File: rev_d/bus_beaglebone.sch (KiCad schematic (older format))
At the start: 47 parts, among them J1 TERMINATE_JUMPER, J2 LED_JUMPER, SW1 MJTP1243, U1 MCP7940, U2 74HCT08, U3 MCP2562, U4 L78L05AC, U5 ATMEGA324_DIP40, U6 L78L33AC, X1 16MHz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

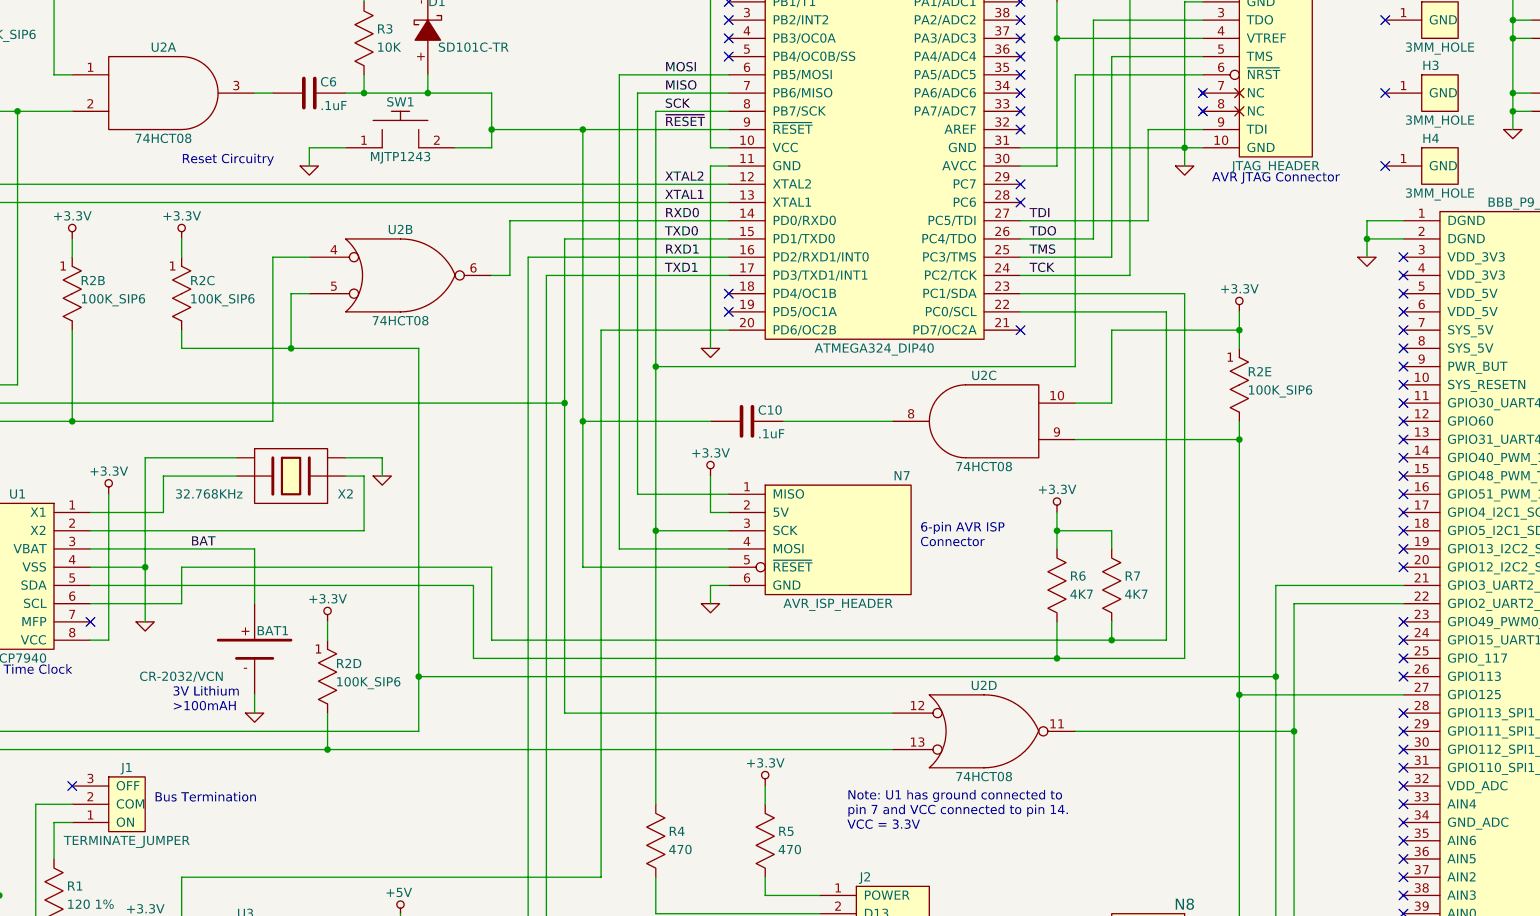
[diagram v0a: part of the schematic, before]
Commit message: Converted 74HCT08 => 74HC08.
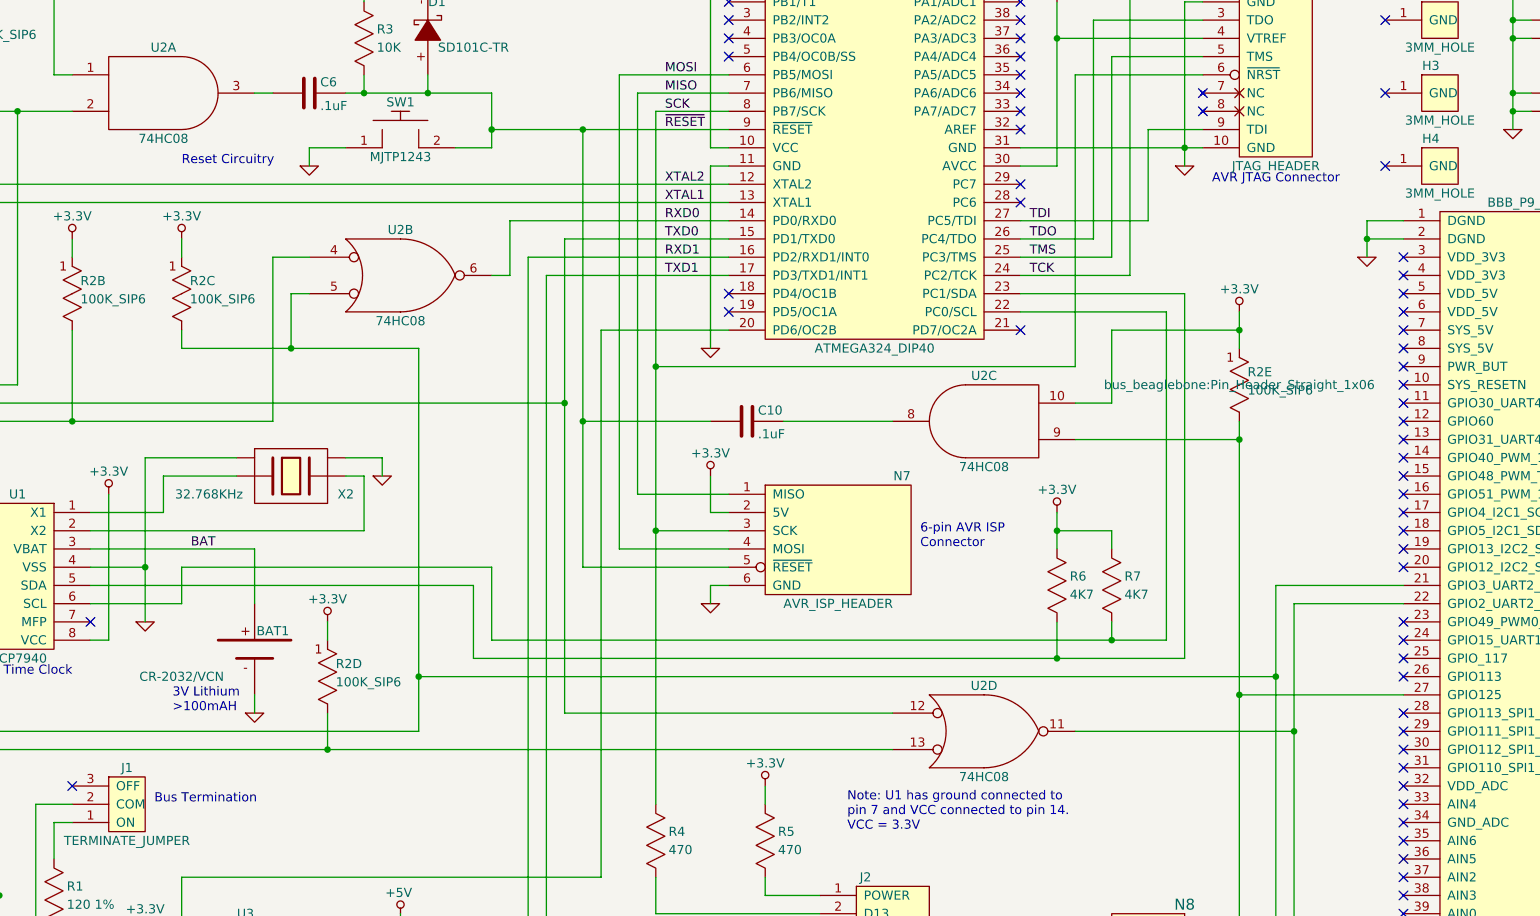
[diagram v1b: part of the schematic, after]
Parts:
- R2: footprint ~ -> bus_beaglebone:Pin_Header_Straight_1x06
- U2: value 74HCT08 -> 74HC08
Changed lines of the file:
@@
 $EndComp
 $Comp
-L GND #PWR02
+L GND #PWR01
 U 1 1 53E3C25F
 P 8100 1900
-F 0 "#PWR02" H 8100 1900 30  0001 C CNN
+F 0 "#PWR01" H 8100 1900 30  0001 C CNN
 F 1 "GND" H 8100 1830 30  0001 C CNN
 F 2 "" H 8100 1900 60  0000 C CNN
@@
 $EndComp
 $Comp
-L GND #PWR03
+L GND #PWR02
 U 1 1 53E3C850
 P 600 2700
-F 0 "#PWR03" H 600 2700 30  0001 C CNN
+F 0 "#PWR02" H 600 2700 30  0001 C CNN
 F 1 "GND" H 600 2630 30  0001 C CNN
 F 2 "" H 600 2700 60  0000 C CNN
@@
 $EndComp
 $Comp
-L GND #PWR04
+L GND #PWR03
 U 1 1 53E3C865
 P 1400 2700
-F 0 "#PWR04" H 1400 2700 30  0001 C CNN
+F 0 "#PWR03" H 1400 2700 30  0001 C CNN
 F 1 "GND" H 1400 2630 30  0001 C CNN
 F 2 "" H 1400 2700 60  0000 C CNN
@@
 $EndComp
 $Comp
-L GND #PWR05
+L GND #PWR04
 U 1 1 53E3ED67
 P 3950 6500
-F 0 "#PWR05" H 3950 6500 30  0001 C CNN
+F 0 "#PWR04" H 3950 6500 30  0001 C CNN
 F 1 "GND" H 3950 6430 30  0001 C CNN
 F 2 "" H 3950 6500 60  0000 C CNN
@@
 $EndComp
 $Comp
-L GND #PWR06
+L GND #PWR05
 U 1 1 53E4026A
 P 1400 5500
-F 0 "#PWR06" H 1400 5500 30  0001 C CNN
+F 0 "#PWR05" H 1400 5500 30  0001 C CNN
 F 1 "GND" H 1400 5430 30  0001 C CNN
 F 2 "" H 1400 5500 60  0000 C CNN
@@
 $EndComp
 $Comp
-L GND #PWR07
+L GND #PWR06
 U 1 1 53E406BF
 P 1400 3700
-F 0 "#PWR07" H 1400 3700 30  0001 C CNN
+F 0 "#PWR06" H 1400 3700 30  0001 C CNN
 F 1 "GND" H 1400 3630 30  0001 C CNN
 F 2 "" H 1400 3700 60  0000 C CNN
@@
 P 3800 2500
 F 0 "U2" H 3800 2750 50  0000 C CNN
-F 1 "74HCT08" H 3800 2250 50  0000 C CNN
+F 1 "74HC08" H 3800 2250 50  0000 C CNN
 F 2 "bus_beaglebone:DIP-14__300" H 3800 2500 60  0001 C CNN
 F 3 "" H 3800 2500 60  0000 C CNN
@@
 P 7000 5000
 F 0 "U2" H 7000 5250 50  0000 C CNN
-F 1 "74HCT08" H 7000 4750 50  0000 C CNN
+F 1 "74HC08" H 7000 4750 50  0000 C CNN
 F 2 "bus_beaglebone:DIP-14__300" H 7000 5000 60  0001 C CNN
 F 3 "" H 7000 5000 60  0000 C CNN
@@
 $EndComp
 $Comp
-L GND #PWR08
+L GND #PWR07
 U 1 1 53E41588
 P 8500 6500
-F 0 "#PWR08" H 8500 6500 30  0001 C CNN
+F 0 "#PWR07" H 8500 6500 30  0001 C CNN
 F 1 "GND" H 8500 6430 30  0001 C CNN
 F 2 "" H 8500 6500 60  0000 C CNN
@@
 NoConn ~ -2850 4150
 $Comp
-L GND #PWR09
+L GND #PWR08
 U 1 1 53E4BEB5
 P 3300 1900
-F 0 "#PWR09" H 3300 1900 30  0001 C CNN
+F 0 "#PWR08" H 3300 1900 30  0001 C CNN
 F 1 "GND" H 3300 1830 30  0001 C CNN
 F 2 "" H 3300 1900 60  0000 C CNN
@@
 $EndComp
 $Comp
-L GND #PWR010
+L GND #PWR09
 U 1 1 53E4C9AF
 P 5500 2900
-F 0 "#PWR010" H 5500 2900 30  0001 C CNN
+F 0 "#PWR09" H 5500 2900 30  0001 C CNN
 F 1 "GND" H 5500 2830 30  0001 C CNN
 F 2 "" H 5500 2900 60  0000 C CNN
@@
 $EndComp
 $Comp
-L GND #PWR011
+L GND #PWR010
 U 1 1 53E42028
 P 5500 4300
-F 0 "#PWR011" H 5500 4300 30  0001 C CNN
+F 0 "#PWR010" H 5500 4300 30  0001 C CNN
 F 1 "GND" H 5500 4230 30  0001 C CNN
 F 2 "" H 5500 4300 60  0000 C CNN
@@
 NoConn ~ 7200 1700
 $Comp
-L +5V #PWR012
+L +5V #PWR011
 U 1 1 53E5079A
 P 2800 7000
-F 0 "#PWR012" H 2800 7090 20  0001 C CNN
+F 0 "#PWR011" H 2800 7090 20  0001 C CNN
 F 1 "+5V" H 2790 7115 50  0000 C CNN
 F 2 "" H 2800 7000 60  0000 C CNN
@@
 $EndComp
 $Comp
-L GND #PWR013
+L GND #PWR012
 U 1 1 53E64F41
 P 6000 6900
-F 0 "#PWR013" H 6000 6900 30  0001 C CNN
+F 0 "#PWR012" H 6000 6900 30  0001 C CNN
 F 1 "GND" H 6000 6830 30  0001 C CNN
 F 2 "" H 6000 6900 60  0000 C CNN
@@
 P 2500 1500
 F 0 "U2" H 2500 1750 50  0000 C CNN
-F 1 "74HCT08" H 2500 1250 50  0000 C CNN
+F 1 "74HC08" H 2500 1250 50  0000 C CNN
 F 2 "bus_beaglebone:DIP-14__300" H 2500 1500 60  0001 C CNN
 F 3 "" H 2500 1500 60  0000 C CNN
@@
 P 7000 3300
 F 0 "U2" H 7000 3050 50  0000 C CNN
-F 1 "74HCT08" H 7000 3550 50  0000 C CNN
+F 1 "74HC08" H 7000 3550 50  0000 C CNN
 F 2 "bus_beaglebone:DIP-14__300" H 7000 3300 60  0001 C CNN
 F 3 "" H 7000 3300 60  0000 C CNN
@@
 $EndComp
 $Comp
-L GND #PWR014
+L GND #PWR013
 U 1 1 53E8748B
 P 9100 2400
-F 0 "#PWR014" H 9100 2400 30  0001 C CNN
+F 0 "#PWR013" H 9100 2400 30  0001 C CNN
 F 1 "GND" H 9100 2330 30  0001 C CNN
 F 2 "" H 9100 2400 60  0000 C CNN
@@
 $EndComp
 $Comp
-L GND #PWR015
+L GND #PWR014
 U 1 1 5443768F
 P 3000 4900
-F 0 "#PWR015" H 3000 4900 30  0001 C CNN
+F 0 "#PWR014" H 3000 4900 30  0001 C CNN
 F 1 "GND" H 3000 4830 30  0001 C CNN
 F 2 "" H 3000 4900 60  0000 C CNN
@@
 $EndComp
 $Comp
-L GND #PWR016
+L GND #PWR015
 U 1 1 5443780C
 P 2400 4400
-F 0 "#PWR016" H 2400 4400 30  0001 C CNN
+F 0 "#PWR015" H 2400 4400 30  0001 C CNN
 F 1 "GND" H 2400 4330 30  0001 C CNN
 F 2 "" H 2400 4400 60  0000 C CNN
@@
 $EndComp
 $Comp
-L +3.3V #PWR017
+L +3.3V #PWR016
 U 1 1 5443A36B
 P 7400 3800
-F 0 "#PWR017" H 7400 3760 30  0001 C CNN
+F 0 "#PWR016" H 7400 3760 30  0001 C CNN
 F 1 "+3.3V" H 7400 3925 50  0000 C CNN
 F 2 "" H 7400 3800 60  0000 C CNN
@@
 $EndComp
 $Comp
-L +3.3V #PWR018
+L +3.3V #PWR017
 U 1 1 5443A423
 P 8400 2700
-F 0 "#PWR018" H 8400 2660 30  0001 C CNN
+F 0 "#PWR017" H 8400 2660 30  0001 C CNN
 F 1 "+3.3V" H 8400 2825 50  0000 C CNN
 F 2 "" H 8400 2700 60  0000 C CNN
@@
 $EndComp
 $Comp
-L +3.3V #PWR019
+L +3.3V #PWR018
 U 1 1 5443A4D3
 P 2200 3700
-F 0 "#PWR019" H 2200 3660 30  0001 C CNN
+F 0 "#PWR018" H 2200 3660 30  0001 C CNN
 F 1 "+3.3V" H 2200 3825 50  0000 C CNN
 F 2 "" H 2200 3700 60  0000 C CNN
@@
 GND
 $Comp
-L GND #PWR020
+L GND #PWR019
 U 1 1 54441157
 P 3700 3600
-F 0 "#PWR020" H 3700 3600 30  0001 C CNN
+F 0 "#PWR019" H 3700 3600 30  0001 C CNN
 F 1 "GND" H 3700 3530 30  0001 C CNN
 F 2 "" H 3700 3600 60  0000 C CNN
@@
 $EndComp
 $Comp
-L GND #PWR021
+L GND #PWR020
 U 1 1 54442992
 P 9900 1700
-F 0 "#PWR021" H 9900 1700 30  0001 C CNN
+F 0 "#PWR020" H 9900 1700 30  0001 C CNN
 F 1 "GND" H 9900 1630 30  0001 C CNN
 F 2 "" H 9900 1700 60  0000 C CNN
@@
 $EndComp
 $Comp
-L +3.3V #PWR022
+L +3.3V #PWR021
 U 1 1 54ADFC43
 P 7400 1000
-F 0 "#PWR022" H 7400 960 30  0001 C CNN
+F 0 "#PWR021" H 7400 960 30  0001 C CNN
 F 1 "+3.3V" H 7400 1125 50  0000 C CNN
 F 2 "" H 7400 1000 60  0000 C CNN
@@
 NoConn ~ 9300 2500
 $Comp
-L +3.3V #PWR023
+L +3.3V #PWR022
 U 1 1 54AE0541
 P 3950 700
-F 0 "#PWR023" H 3950 660 30  0001 C CNN
+F 0 "#PWR022" H 3950 660 30  0001 C CNN
 F 1 "+3.3V" H 3950 825 50  0000 C CNN
 F 2 "" H 3950 700 60  0000 C CNN
@@
 $EndComp
 $Comp
-L +3.3V #PWR024
+L +3.3V #PWR023
 U 1 1 54AE0CA5
 P 1400 850
-F 0 "#PWR024" H 1400 810 30  0001 C CNN
+F 0 "#PWR023" H 1400 810 30  0001 C CNN
 F 1 "+3.3V" H 1400 975 50  0000 C CNN
 F 2 "" H 1400 850 60  0000 C CNN
@@
 $EndComp
 $Comp
-L +3.3V #PWR025
+L +3.3V #PWR024
 U 1 1 54AE0EC4
 P 2000 2300
-F 0 "#PWR025" H 2000 2260 30  0001 C CNN
+F 0 "#PWR024" H 2000 2260 30  0001 C CNN
 F 1 "+3.3V" H 2000 2425 50  0000 C CNN
 F 2 "" H 2000 2300 60  0000 C CNN
@@
 $EndComp
 $Comp
-L +3.3V #PWR026
+L +3.3V #PWR025
 U 1 1 54AE1BC8
 P 2400 6100
-F 0 "#PWR026" H 2400 6060 30  0001 C CNN
+F 0 "#PWR025" H 2400 6060 30  0001 C CNN
 F 1 "+3.3V" H 2400 6225 50  0000 C CNN
 F 2 "" H 2400 6100 60  0000 C CNN
@@
 $EndComp
 $Comp
-L +3.3V #PWR027
+L +3.3V #PWR026
 U 1 1 54AE24EE
 P 5500 3600
-F 0 "#PWR027" H 5500 3560 30  0001 C CNN
+F 0 "#PWR026" H 5500 3560 30  0001 C CNN
 F 1 "+3.3V" H 5500 3725 50  0000 C CNN
 F 2 "" H 5500 3600 60  0000 C CNN
@@
 $EndComp
 $Comp
-L +3.3V #PWR028
+L +3.3V #PWR027
 U 1 1 54AE4768
 P 5800 5300
-F 0 "#PWR028" H 5800 5260 30  0001 C CNN
+F 0 "#PWR027" H 5800 5260 30  0001 C CNN
 F 1 "+3.3V" H 5800 5425 50  0000 C CNN
 F 2 "" H 5800 5300 60  0000 C CNN
@@
 NoConn ~ 9300 4100
 $Comp
-L +3.3V #PWR029
+L +3.3V #PWR028
 U 1 1 54AE64E0
 P 2600 2300
-F 0 "#PWR029" H 2600 2260 30  0001 C CNN
+F 0 "#PWR028" H 2600 2260 30  0001 C CNN
 F 1 "+3.3V" H 2600 2425 50  0000 C CNN
 F 2 "" H 2600 2300 60  0000 C CNN
@@
 $EndComp
 $Comp
-L GND #PWR030
+L GND #PWR029
 U 1 1 54AE368F
 P 2800 7800
-F 0 "#PWR030" H 2800 7800 30  0001 C CNN
+F 0 "#PWR029" H 2800 7800 30  0001 C CNN
 F 1 "GND" H 2800 7730 30  0001 C CNN
 F 2 "" H 2800 7800 60  0000 C CNN
@@
 Extra Serial Connector
 $Comp
-L +3.3V #PWR031
+L +3.3V #PWR030
 U 1 1 54AE44C6
 P 4600 7000
-F 0 "#PWR031" H 4600 6960 30  0001 C CNN
+F 0 "#PWR030" H 4600 6960 30  0001 C CNN
 F 1 "+3.3V" H 4600 7125 50  0000 C CNN
 F 2 "" H 4600 7000 60  0000 C CNN
@@
 $EndComp
 $Comp
-L +5V #PWR032
+L +5V #PWR031
 U 1 1 54B30DFF
 P 3800 6000
-F 0 "#PWR032" H 3800 6090 20  0001 C CNN
+F 0 "#PWR031" H 3800 6090 20  0001 C CNN
 F 1 "+5V" H 3790 6115 50  0000 C CNN
 F 2 "" H 3800 6000 60  0000 C CNN
@@
 $EndComp
 $Comp
-L +3.3V #PWR033
+L +3.3V #PWR032
 U 1 1 54B37C19
 P 3400 4400
-F 0 "#PWR033" H 3400 4360 30  0001 C CNN
+F 0 "#PWR032" H 3400 4360 30  0001 C CNN
 F 1 "+3.3V" H 3400 4525 50  0000 C CNN
 F 2 "" H 3400 4400 60  0000 C CNN
@@
 F 0 "R2" H 8445 3170 50  0000 L CNN
 F 1 "100K_SIP6" H 8445 3070 50  0000 L CNN
-F 2 "~" H 8400 3100 50  0000 C CNN
+F 2 "bus_beaglebone:Pin_Header_Straight_1x06" H 8400 3100 50  0000 C CNN
 F 3 "" H 8400 3100 50  0000 C CNN
 	5    8400 3100
